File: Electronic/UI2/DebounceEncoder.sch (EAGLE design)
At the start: 28 parts, among them IC1 74HCT14N, IC2 74HCT14N, IC3 74LS74N

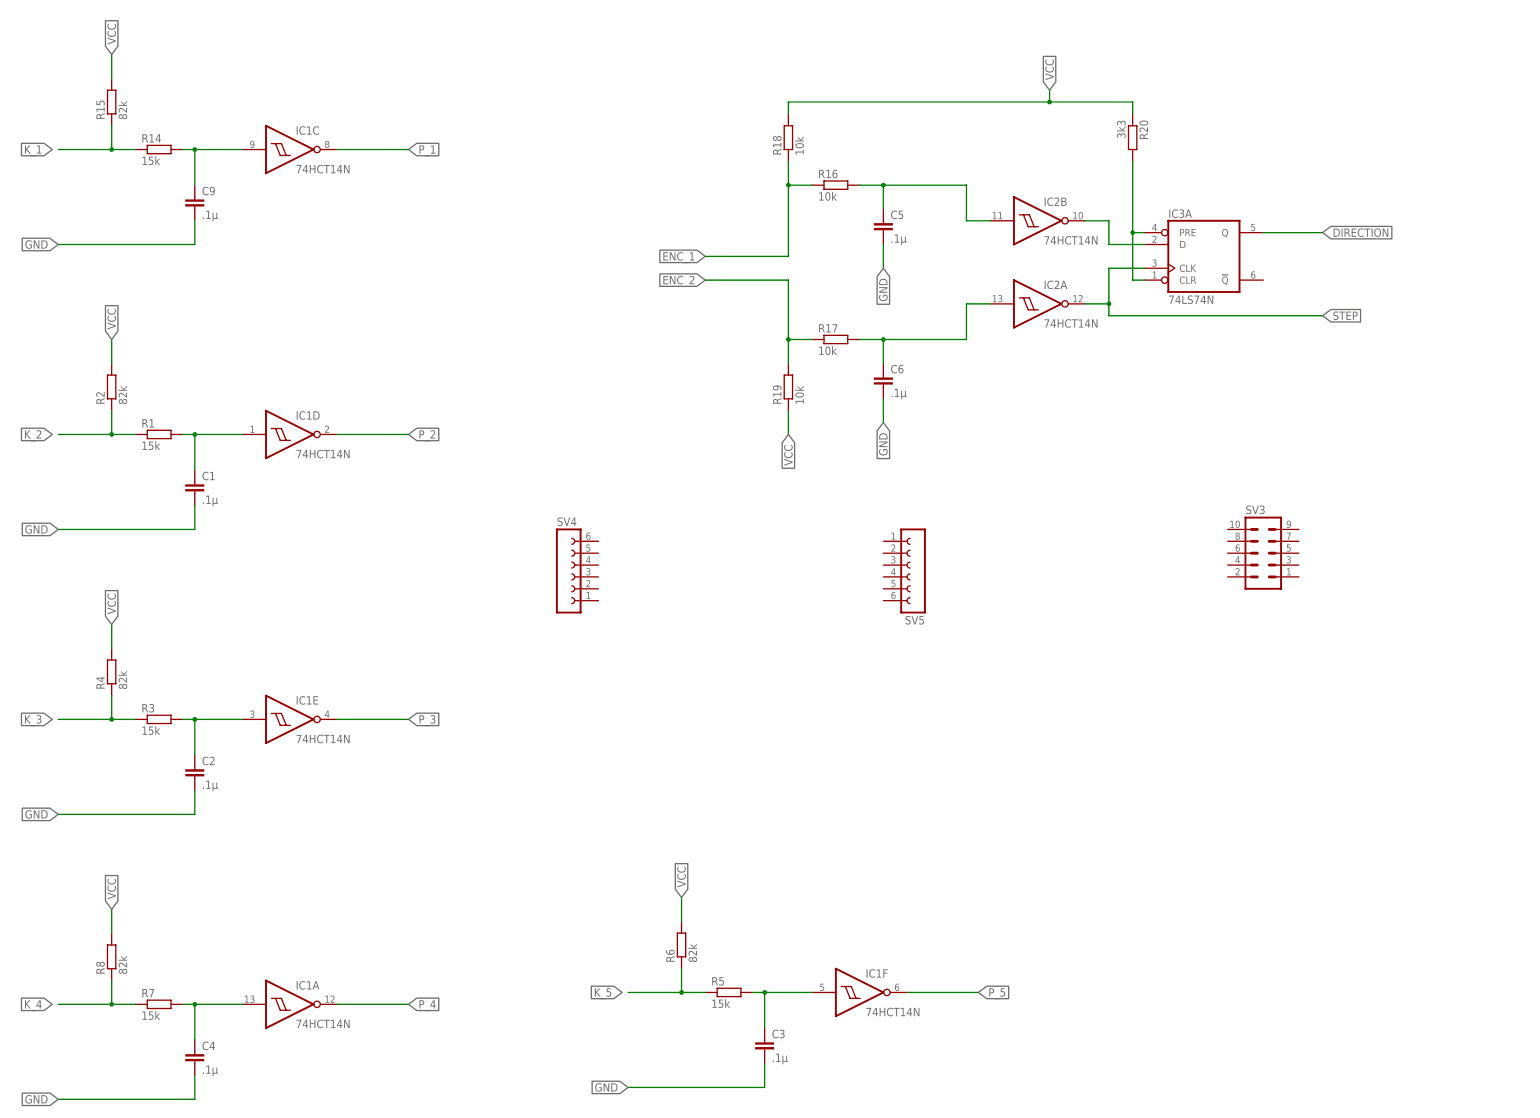
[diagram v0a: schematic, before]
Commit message: Updated connectors
and more work on the UI Boards
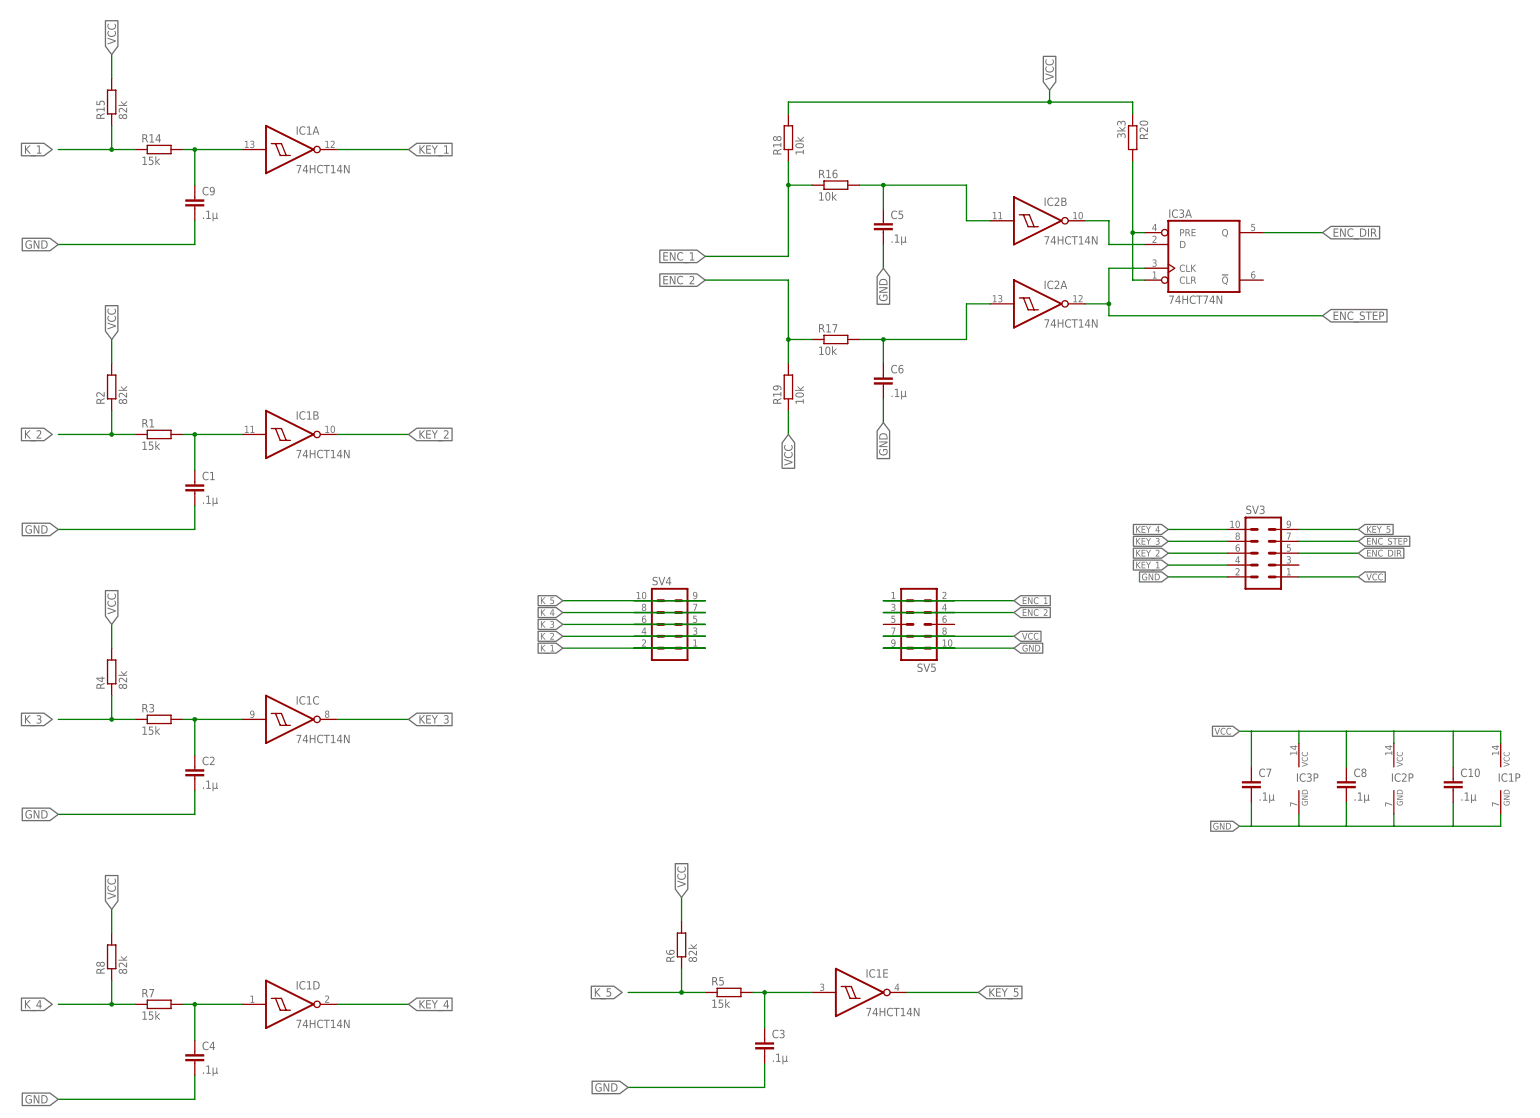
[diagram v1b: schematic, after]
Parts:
- added C10, C7, C8: .1µ, rcl:C-EU025-024X044
- IC3: value 74LS74N -> 74HCT74N; device 74xx-eu:74LS74N -> 74xx-eu:74HCT74N
- SV4, SV5: device con-lsta:FE06-1 -> con-lstb:MA05-2
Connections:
- removed net DIRECTION: IC3A.Q
- removed net P_1: IC1C.O
- removed net P_2: IC1D.O
- removed net P_3: IC1E.O
- removed net P_4: IC1A.O
- removed net P_5: IC1F.O
- removed net STEP: IC2A.O, IC3A.CLK
- new net ENC_DIR: IC3A.Q, SV3.5
- new net ENC_STEP: IC2A.O, IC3A.CLK, SV3.7
- new net KEY_1: IC1A.O, SV3.4
- new net KEY_2: IC1B.O, SV3.6
- new net KEY_3: IC1C.O, SV3.8
- new net KEY_4: IC1D.O, SV3.10
- new net KEY_5: IC1E.O, SV3.9
- net ENC_1: now also SV5.1, SV5.2
- net ENC_2: now also SV5.3, SV5.4
- net GND: now also C10.2, C7.2, C8.2, IC1P.GND, IC2P.GND, IC3P.GND, SV3.2, SV5.10, SV5.9
- net K1: now also IC1A.I; no longer IC1C.I
- net K2: now also IC1B.I; no longer IC1D.I
- net K3: now also IC1C.I; no longer IC1E.I
- net K4: now also IC1E.I; no longer IC1F.I
- net K5: now also IC1D.I; no longer IC1A.I
- net K_1: now also SV4.1, SV4.2
- net K_2: now also SV4.3, SV4.4
- net K_3: now also SV4.5, SV4.6
- net K_4: now also SV4.7, SV4.8
- net K_5: now also SV4.10, SV4.9
- net VCC: now also C10.1, C7.1, C8.1, IC1P.VCC, IC2P.VCC, IC3P.VCC, SV3.1, SV5.7, SV5.8
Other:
- moved on the sheet: IC1A, IC1C, IC1D, IC1E

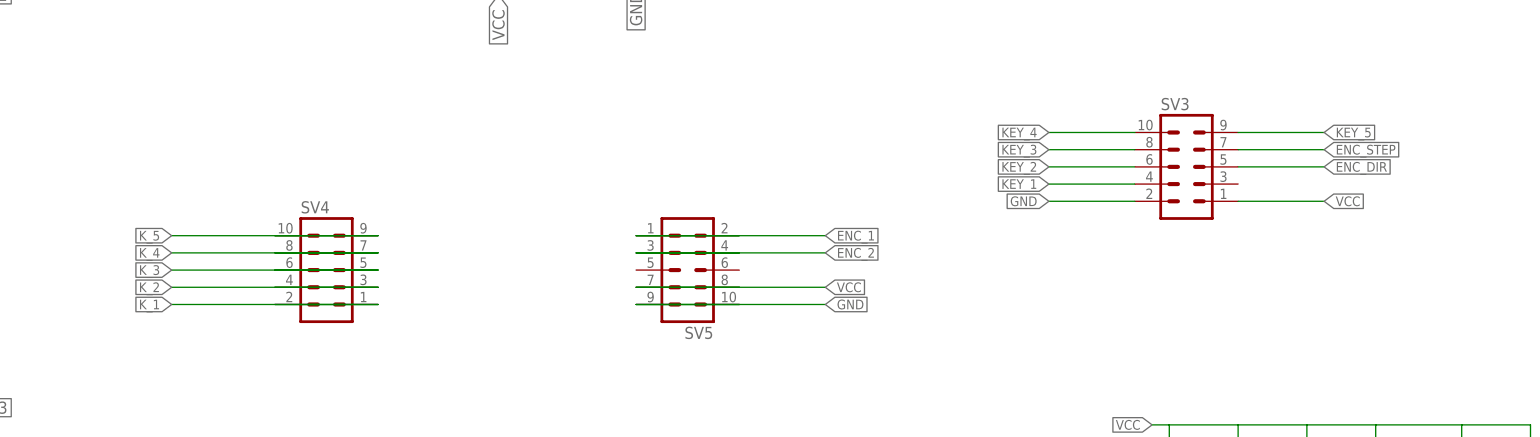
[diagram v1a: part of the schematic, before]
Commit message: new Keycross and EC60A board
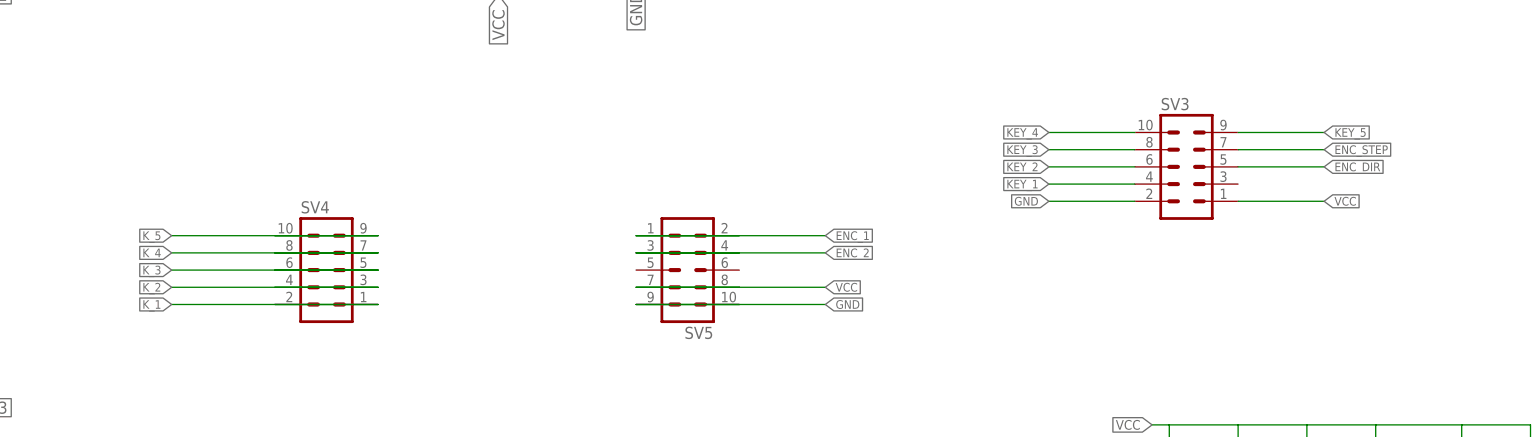
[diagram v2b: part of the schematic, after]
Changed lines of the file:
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@@
 <wire x1="220.98" y1="111.76" x2="205.74" y2="111.76" width="0.1524" layer="91"/>
 <wire x1="205.74" y1="111.76" x2="233.68" y2="111.76" width="0.1524" layer="91"/>
-<label x="233.68" y="111.76" size="1.4224" layer="95" xref="yes"/>
+<label x="233.68" y="111.76" size="1.27" layer="95" xref="yes"/>
 </segment>
 <segment>
 <pinref part="SV3" gate="G$1" pin="1"/>
 <wire x1="294.64" y1="124.46" x2="307.34" y2="124.46" width="0.1524" layer="91"/>
-<label x="307.34" y="124.46" size="1.4224" layer="95" xref="yes"/>
+<label x="307.34" y="124.46" size="1.27" layer="95" xref="yes"/>
 </segment>
 <segment>
@@
 <wire x1="220.98" y1="109.22" x2="205.74" y2="109.22" width="0.1524" layer="91"/>
 <wire x1="205.74" y1="109.22" x2="233.68" y2="109.22" width="0.1524" layer="91"/>
-<label x="233.68" y="109.22" size="1.4224" layer="95" xref="yes"/>
+<label x="233.68" y="109.22" size="1.27" layer="95" xref="yes"/>
 </segment>
 <segment>
 <pinref part="SV3" gate="G$1" pin="2"/>
 <wire x1="279.4" y1="124.46" x2="266.7" y2="124.46" width="0.1524" layer="91"/>
-<label x="266.7" y="124.46" size="1.4224" layer="95" rot="R180" xref="yes"/>
+<label x="266.7" y="124.46" size="1.27" layer="95" rot="R180" xref="yes"/>
 </segment>
 <segment>
@@
 <wire x1="167.64" y1="109.22" x2="152.4" y2="109.22" width="0.1524" layer="91"/>
 <wire x1="167.64" y1="109.22" x2="137.16" y2="109.22" width="0.1524" layer="91"/>
-<label x="137.16" y="109.22" size="1.4224" layer="95" rot="R180" xref="yes"/>
+<label x="137.16" y="109.22" size="1.27" layer="95" rot="R180" xref="yes"/>
 </segment>
 </net>
@@
 <wire x1="220.98" y1="119.38" x2="205.74" y2="119.38" width="0.1524" layer="91"/>
 <wire x1="205.74" y1="119.38" x2="233.68" y2="119.38" width="0.1524" layer="91"/>
-<label x="233.68" y="119.38" size="1.4224" layer="95" xref="yes"/>
+<label x="233.68" y="119.38" size="1.27" layer="95" xref="yes"/>
 </segment>
 </net>
@@
 <wire x1="220.98" y1="116.84" x2="205.74" y2="116.84" width="0.1524" layer="91"/>
 <wire x1="205.74" y1="116.84" x2="233.68" y2="116.84" width="0.1524" layer="91"/>
-<label x="233.68" y="116.84" size="1.4224" layer="95" xref="yes"/>
+<label x="233.68" y="116.84" size="1.27" layer="95" xref="yes"/>
 </segment>
 </net>
@@
 <pinref part="SV4" gate="G$1" pin="4"/>
 <wire x1="167.64" y1="111.76" x2="152.4" y2="111.76" width="0.1524" layer="91"/>
-<label x="137.16" y="111.76" size="1.4224" layer="95" rot="R180" xref="yes"/>
+<label x="137.16" y="111.76" size="1.27" layer="95" rot="R180" xref="yes"/>
 </segment>
 </net>
@@
 <wire x1="152.4" y1="114.3" x2="167.64" y2="114.3" width="0.1524" layer="91"/>
 <wire x1="167.64" y1="114.3" x2="137.16" y2="114.3" width="0.1524" layer="91"/>
-<label x="137.16" y="114.3" size="1.4224" layer="95" rot="R180" xref="yes"/>
+<label x="137.16" y="114.3" size="1.27" layer="95" rot="R180" xref="yes"/>
 </segment>
 </net>
@@
 <pinref part="SV4" gate="G$1" pin="8"/>
 <wire x1="167.64" y1="116.84" x2="152.4" y2="116.84" width="0.1524" layer="91"/>
-<label x="137.16" y="116.84" size="1.4224" layer="95" rot="R180" xref="yes"/>
+<label x="137.16" y="116.84" size="1.27" layer="95" rot="R180" xref="yes"/>
 </segment>
 </net>
@@
 <wire x1="152.4" y1="119.38" x2="167.64" y2="119.38" width="0.1524" layer="91"/>
 <wire x1="167.64" y1="119.38" x2="137.16" y2="119.38" width="0.1524" layer="91"/>
-<label x="137.16" y="119.38" size="1.4224" layer="95" rot="R180" xref="yes"/>
+<label x="137.16" y="119.38" size="1.27" layer="95" rot="R180" xref="yes"/>
 </segment>
 </net>
@@
 <pinref part="SV3" gate="G$1" pin="4"/>
 <wire x1="266.7" y1="127" x2="279.4" y2="127" width="0.1524" layer="91"/>
-<label x="266.7" y="127" size="1.4224" layer="95" rot="R180" xref="yes"/>
+<label x="266.7" y="127" size="1.27" layer="95" rot="R180" xref="yes"/>
 </segment>
 <segment>
@@
 <pinref part="SV3" gate="G$1" pin="6"/>
 <wire x1="279.4" y1="129.54" x2="266.7" y2="129.54" width="0.1524" layer="91"/>
-<label x="266.7" y="129.54" size="1.4224" layer="95" rot="R180" xref="yes"/>
+<label x="266.7" y="129.54" size="1.27" layer="95" rot="R180" xref="yes"/>
 </segment>
 <segment>
@@
 <pinref part="SV3" gate="G$1" pin="8"/>
 <wire x1="266.7" y1="132.08" x2="279.4" y2="132.08" width="0.1524" layer="91"/>
-<label x="266.7" y="132.08" size="1.4224" layer="95" rot="R180" xref="yes"/>
+<label x="266.7" y="132.08" size="1.27" layer="95" rot="R180" xref="yes"/>
 </segment>
 <segment>
@@
 <pinref part="SV3" gate="G$1" pin="10"/>
 <wire x1="279.4" y1="134.62" x2="266.7" y2="134.62" width="0.1524" layer="91"/>
-<label x="266.7" y="134.62" size="1.4224" layer="95" rot="R180" xref="yes"/>
+<label x="266.7" y="134.62" size="1.27" layer="95" rot="R180" xref="yes"/>
 </segment>
 <segment>
@@
 <pinref part="SV3" gate="G$1" pin="9"/>
 <wire x1="294.64" y1="134.62" x2="307.34" y2="134.62" width="0.1524" layer="91"/>
-<label x="307.34" y="134.62" size="1.4224" layer="95" xref="yes"/>
+<label x="307.34" y="134.62" size="1.27" layer="95" xref="yes"/>
 </segment>
 <segment>
@@
 <pinref part="SV3" gate="G$1" pin="7"/>
 <wire x1="294.64" y1="132.08" x2="307.34" y2="132.08" width="0.1524" layer="91"/>
-<label x="307.34" y="132.08" size="1.4224" layer="95" xref="yes"/>
+<label x="307.34" y="132.08" size="1.27" layer="95" xref="yes"/>
 </segment>
 <segment>
@@
 <pinref part="SV3" gate="G$1" pin="5"/>
 <wire x1="294.64" y1="129.54" x2="307.34" y2="129.54" width="0.1524" layer="91"/>
-<label x="307.34" y="129.54" size="1.4224" layer="95" xref="yes"/>
-</segment>
-<segment>
+<label x="307.34" y="129.54" size="1.27" layer="95" xref="yes"/>
+</segment>
+<segment>
